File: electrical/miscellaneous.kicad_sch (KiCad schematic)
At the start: 1 part

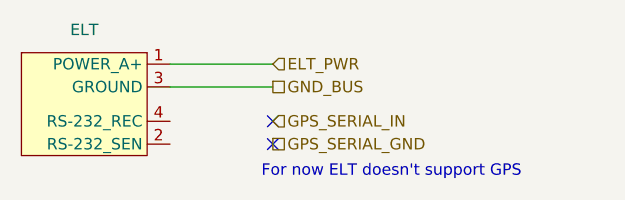
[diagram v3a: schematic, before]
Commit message: Changed to have ELT with GPS. Also, changed Flaps to have position sensor. Added in wiring for all the sensors.
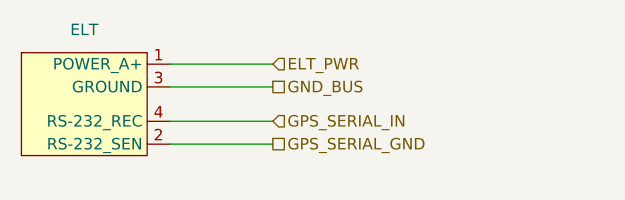
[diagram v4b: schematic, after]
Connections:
- net GPS_SERIAL_GND: now also ELT.2 (RS-232_SEN)
- net GPS_SERIAL_IN: now also ELT.4 (RS-232_REC)
- no-connect marks 2 -> 0
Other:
- note removed: "For now ELT doesn't support GPS"
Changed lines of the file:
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@@
     (company "N877RV")
   )
-  (no_connect (at 147.32 90.17))
-  (no_connect (at 147.32 92.71))
+  (wire (pts (xy 135.89 92.71) (xy 147.32 92.71))
+    (stroke (width 0) (type default))
+  )
   (wire (pts (xy 135.89 86.36) (xy 147.32 86.36))
     (stroke (width 0) (type default))
@@
     (stroke (width 0) (type default))
   )
-  (text "For now ELT doesn't support GPS" (at 146.05 96.52 0)
-    (effects (font (size 1.27 1.27)) (justify left bottom))
+  (wire (pts (xy 135.89 90.17) (xy 147.32 90.17))
+    (stroke (width 0) (type default))
   )
   (hierarchical_label "GPS_SERIAL_GND" (shape passive) (at 147.32 92.71 0) (fields_autoplaced)
